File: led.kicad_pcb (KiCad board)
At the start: 2 copper layers, 100 x 100 mm, 112 parts, among them J1 Slip_ring_48V, J2 Slip_ring_I2C, J3 Analog_input, J4 Test_power, J52 Jump_ID_1, J53 Jump_ID_2, J54 Test_Vds, J55 Test_sense, J56 Jump_ID_3, J57 Jump_ID_4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

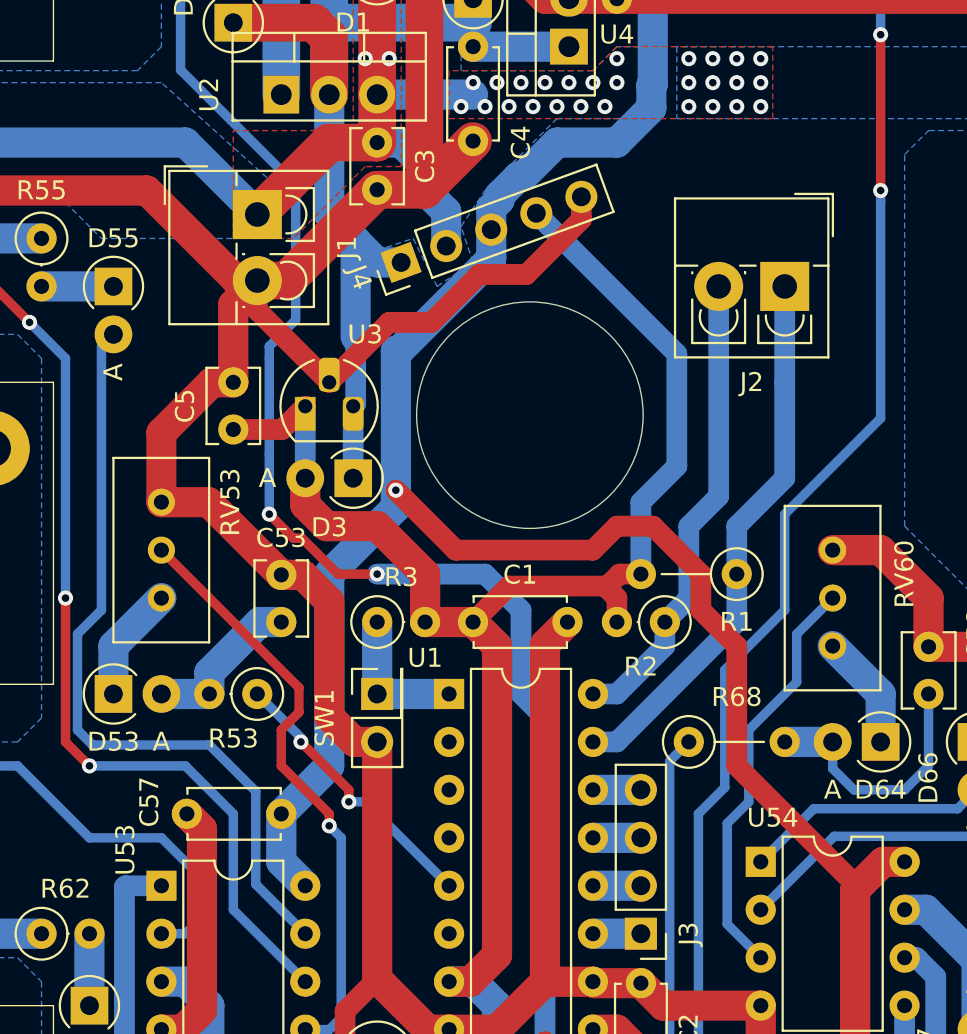
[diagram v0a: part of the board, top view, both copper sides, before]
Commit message: PCB: Add more silks
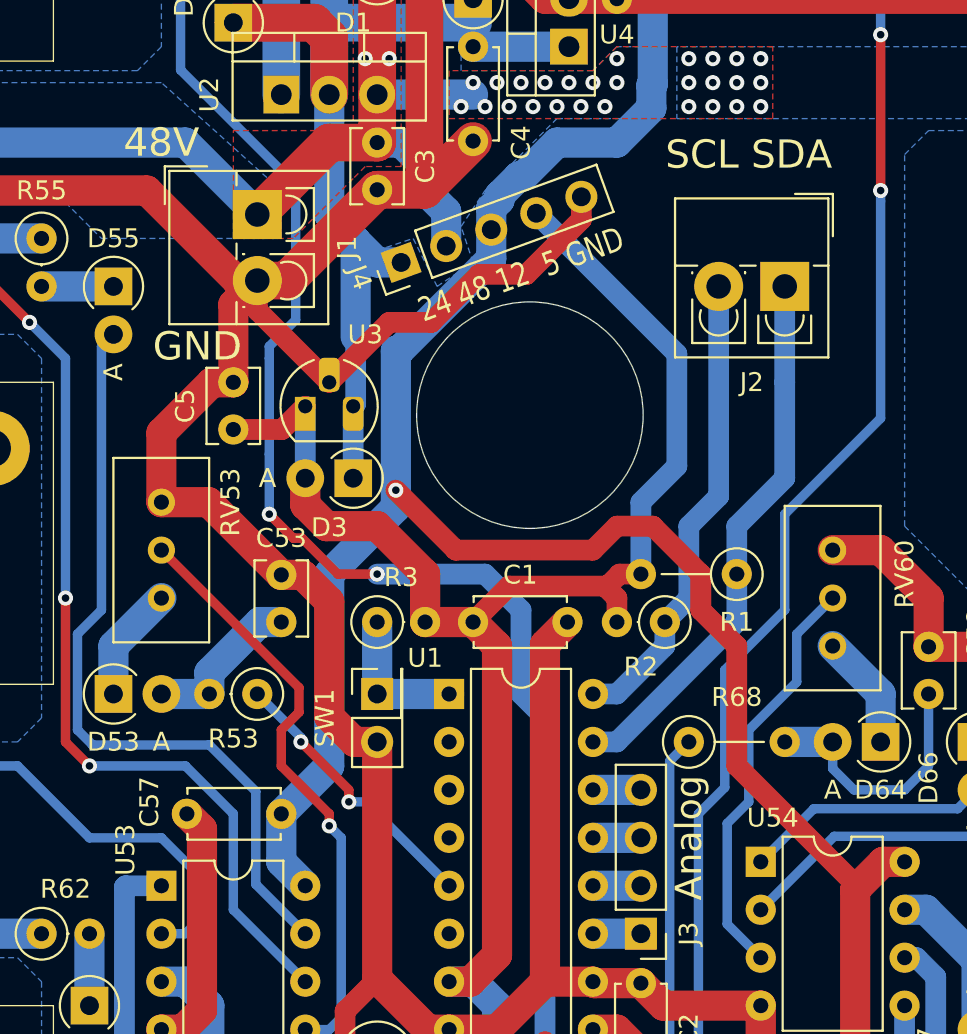
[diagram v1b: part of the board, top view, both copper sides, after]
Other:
- board text added: "24 48 12 5 GND"
- board text added: "48V"
- board text added: "Analog"
- board text added: "GND"
- board text added: "LED driver v0.0.0 for the new planetarium projector (c) 2018 Tsukuba Univ. Astronomy Club Designed by Y. Sugizaki (45th)"
- board text added: "SCL SDA"
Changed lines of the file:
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@@
   (general
     (thickness 1.6)
-    (drawings 11)
+    (drawings 17)
     (tracks 628)
     (zones 0)
@@
   )
   (setup
-    (last_trace_width 0.3)
+    (last_trace_width 0.5)
     (user_trace_width 0.5)
     (user_trace_width 1.1)
@@
     )
   )
+  (gr_text "LED driver v0.0.0\n      for the new planetarium projector\n(c) 2018 Tsukuba Univ. Astronomy Club\nDesigned by Y. Sugizaki (45th)" (at 107.315 55.245) (layer F.Mask)
+    (effects (font (size 1 0.6) (thickness 0.1)) (justify left))
+  )
+  (gr_text GND (at 83.185 97.155) (layer F.SilkS)
+    (effects (font (size 1.5 1.5) (thickness 0.2)))
+  )
+  (gr_text 48V (at 81.28 86.36) (layer F.SilkS)
+    (effects (font (size 1.5 1.5) (thickness 0.2)))
+  )
+  (gr_text "SCL SDA" (at 112.395 86.995) (layer F.SilkS)
+    (effects (font (size 1.5 1.5) (thickness 0.2)))
+  )
+  (gr_text Analog (at 109.22 123.19 90) (layer F.SilkS)
+    (effects (font (size 1.4 1.4) (thickness 0.2)))
+  )
+  (gr_text "24 48 12  5 GND" (at 100.33 93.345 20) (layer F.SilkS)
+    (effects (font (size 1.27 1) (thickness 0.2)))
+  )
   (gr_text "M3 mounting holes at (+3, +3)" (at 50.8 40.64) (layer F.Fab)
     (effects (font (size 1.5 1.5) (thickness 0.3)))
@@
   (gr_line (start 150.8 53.3) (end 150.8 148.3) (layer Edge.Cuts) (width 0.1))
   (gr_line (start 53.3 50.8) (end 148.3 50.8) (layer Edge.Cuts) (width 0.1))
-  (via (at 56.515 91.44) (size 0.8) (drill 0.4) (layers F.Cu B.Cu) (net 4))
   (segment (start 87.9 93.67) (end 92.71 88.86) (width 2) (layer F.Cu) (net 1) (status 20))
   (segment (start 86.36 93.67) (end 87.9 93.67) (width 2) (layer F.Cu) (net 1) (status 10))
@@
   (segment (start 106.68 134.62) (end 105.41 133.35) (width 1.6) (layer F.Cu) (net 3))
   (segment (start 105.41 133.35) (end 104.14 133.35) (width 1.6) (layer F.Cu) (net 3) (status 20))
+  (via (at 56.515 91.44) (size 0.8) (drill 0.4) (layers F.Cu B.Cu) (net 4))
   (segment (start 92.71 77.47) (end 92.71 83.82) (width 2) (layer F.Cu) (net 4) (status 30))
   (segment (start 92.71 86.36) (end 92.71 83.82) (width 2) (layer F.Cu) (net 4) (status 30))
